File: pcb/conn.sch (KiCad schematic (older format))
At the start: 6 parts, among them P5 CONN_5X2, P6 CONN_16X2, P7 CONN_16, P8 CONN_32, P9 CONN_32

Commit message: almost finished with pcb design
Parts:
- removed P7: CONN_16, symbol CONN_16
- removed P8, P9: CONN_32, symbol CONN_32
- removed SD1: SD, symbol SD
- added JP10, JP2, JP3, JP4, JP5, JP7, JP8, JP9: JP_SW, JP_SW, symbol JP_SW
- added P2: CONN_16X2, symbol CONN_16X2
- renumbered P6 to P1, P5 to P3
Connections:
- net labels added: 0/MC0, 1/MC1, 10/MC10, 11/MC11, 12/MC12, 13/MC13, 14/MC14, 15/MC15, 16/SCL, 17/SDA, 18/EXTRA, 19/SATUS, 2/MC2, 3/MC3, 4/MC4, 5/MC5, 6/MC6, 7/MC7, 8/MC8, 9/MC9, USBDM0, USBDM1, USBDM2, USBDM3, USBDP0, USBDP1, USBDP2, USBDP3, USB_DM, USB_DP
- net labels removed: 0, 1, 10, 100/FSMC_D15, 11, 12, 13, 14, 15/SDIO_D0, 16/SDIO_D1, 17/SDIO_D2, 18/SDIO_D3, 19/SDIO_CK, 2, 20, 21, 22, 23, 24, 25, 26, 27/SDIO_CMD, 28, 29, 3, 30, 31, 32, 33, 34, 35, 36, 37, 38, 39, 4, 40, 41, 42, 43, 44, 45, 46, 47, 48, 49, 5, 50, 51, 52, 53, 54, 55, 56/FSMC_A0, 57/FSMC_A16, 58/FSMC_D0, 59/FSMC_A1, 6/BUT, 60/FSMC_A17, 61/FSMC_D1, 62/FSMC_A2, 63/FSMC_A18, 64/FSMC_D2, 65/FSMC_A3, 66/FSMC_A19, 67/FSMC_D3, 68/FSMC_A4, 69/FSMC_A20, 7, 70/FSMC_D4, 71/FSMC_A5, 72/FSMC_A21, 73/FSMC_D5, 74/FSMC_A6, 75/FSMC_A22, 76/FSMC_D6, 77/FSMC_A7, 78/FSMC_D7, 79/FSMC_A8, 8, 80/FSMC_NE2, 81/FSMC_D8, 82/FSMC_A9, 83/FSMC_NE3, 84/FSMC_D9, 85/FSMC_A10, 86/FSMC_NWE, 87/FSMC_D10, 88/FSMC_A11, 89/FSMC_NOE, 9, 90/FSMC_D11, 91/FSMC_A12, 92/FSMC_NBL1, 93/FSMC_D12, 94/FSMC_A13, 95/FSMC_NBL0, 96/FSMC_D13, 97/FSMC_A14, 98/FSMC_D14, 99/FSMC_A15, VREF
- wire segments 138 -> 105
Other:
- note added: "Bottom"
- note added: "Top"
- moved on the sheet: P1, P3

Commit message: working on power circuitry
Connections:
- net USBDM0: now also P1.23 (P23)
- net USBDM1: now also P1.25
- net USBDM2: now also P1.27 (P27)
- net USBDM3: now also P1.29 (P29)
- net USBDP0: now also P1.24 (P24)
- net USBDP1: now also P1.26 (P26)
- net USBDP2: now also P1.28 (P28)
- net USBDP3: now also P1.30 (P30)

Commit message: Work on single PCB version.
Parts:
- removed P2: CONN_16X2, symbol CONN_16X2
- added C10, C11, C12, C5, C6, C7, C8, C9, C? (x8): C, symbol C
- added P1: CONN_16X2, symbol CONN_16X2
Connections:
- net 0/MC0: now also C5.1, P1.3 (P3)
- net 1/MC1: now also C?.1, P1.4 (P4)
- net 10/MC10: now also C10.1, P1.13 (P13)
- net 11/MC11: now also C?.1, P1.14 (P14)
- net 12/MC12: now also C11.1, P1.15 (P15)
- net 13/MC13: now also C?.1, P1.16 (P16)
- net 14/MC14: now also C12.1, P1.17 (P17)
- net 15/MC15: now also C?.1, P1.18 (P18)
- net 16/SCL: now also P1.19 (P19)
- net 17/SDA: now also P1.20 (P20)
- net 18/EXTRA: now also P1.21 (P21)
- net 19/SATUS: now also P1.22 (P22)
- net 2/MC2: now also C6.1, P1.5 (P5)
- net 3/MC3: now also C?.1, P1.6 (P6)
- net 4/MC4: now also C7.1, P1.7 (P7)
- net 5/MC5: now also C?.1, P1.8 (P8)
- net 6/MC6: now also C8.1, P1.9 (P9)
- net 7/MC7: now also C?.1, P1.10 (P10)
- net 8/MC8: now also C9.1, P1.11 (P11)
- net 9/MC9: now also C?.1, P1.12 (P12)
- net GND: now also C8.2, C?.2, P1.2 (P2), P1.31 (P31)
- net USBDM0: now also P1.23 (P23)
- net USBDM1: now also P1.25
- net USBDM2: now also P1.27 (P27)
- net USBDM3: now also P1.29 (P29)
- net USBDP0: now also P1.24 (P24)
- net USBDP1: now also P1.26 (P26)
- net USBDP2: now also P1.28 (P28)
- net USBDP3: now also P1.30 (P30)
- net VCC: no longer P1.1 (P1), P1.32 (P32)
- new net: C10.2, C11.2, C12.2, C5.2, C6.2, C7.2, C9.2
- new net: C?.2, C?.2, C?.2, C?.2, C?.2, C?.2, C?.2
- new net VIN: P1.1 (P1), P1.1 (P1), P1.32 (P32), P1.32 (P32)
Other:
- moved on the sheet: JP10, JP2, JP3, JP4, JP5, JP7, JP8, JP9, P1, P3

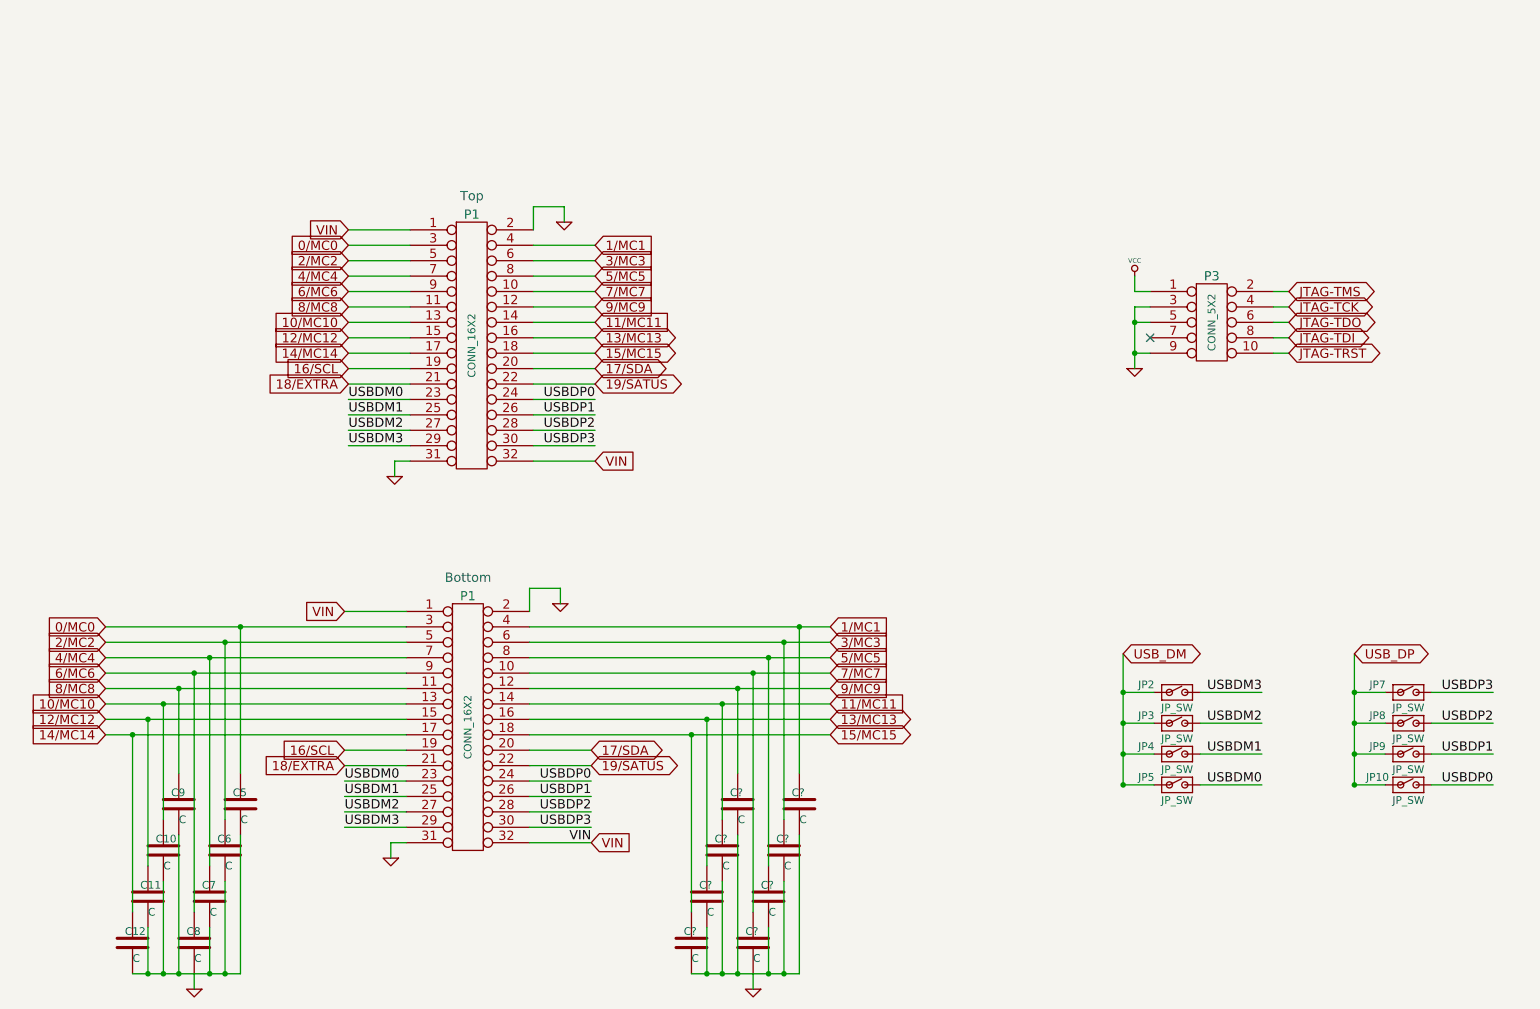
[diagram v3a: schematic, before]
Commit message: Re-routing new, single-board PCB
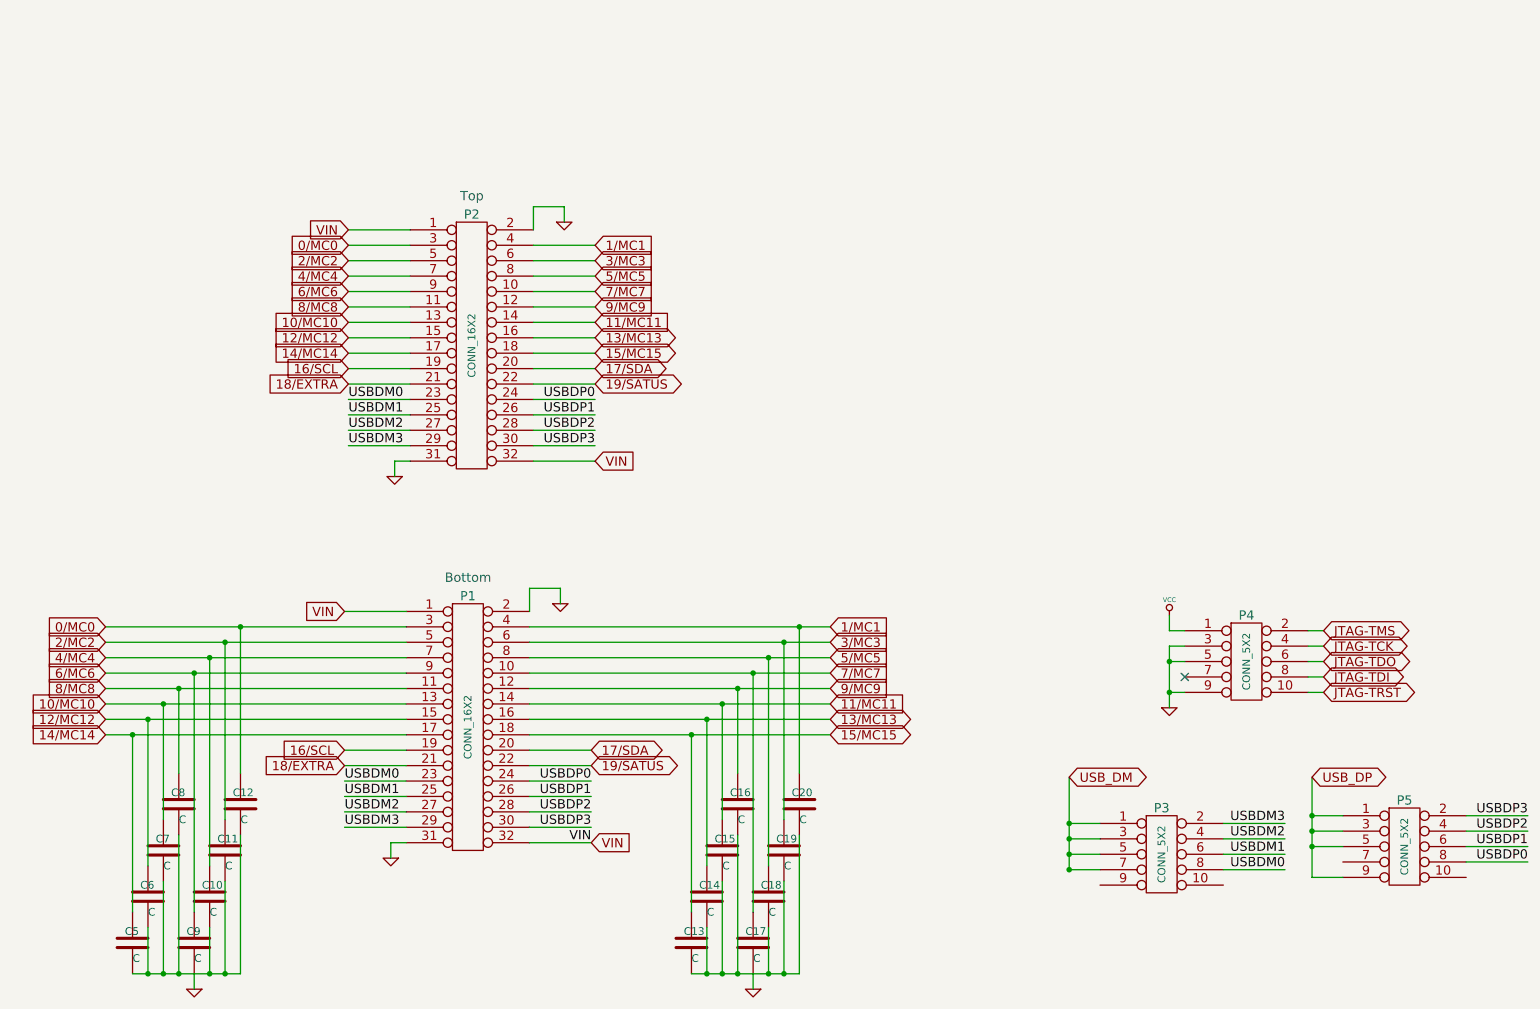
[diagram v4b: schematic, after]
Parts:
- removed JP10, JP2, JP3, JP4, JP5, JP7, JP8, JP9: JP_SW, JP_SW, symbol JP_SW
- added P3, P5: CONN_5X2, symbol CONN_5X2
- gave numbers to parts that had none: 8
- renumbered C7 to C10, C6 to C11, C5 to C12, C12 to C5, C11 to C6, C10 to C7, C9 to C8, C8 to C9, P1 to P2, P3 to P4
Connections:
- net USBDM0: now also P3.8
- net USBDM1: now also P3.6
- net USBDM2: now also P3.4
- net USBDM3: now also P3.2
- net USBDP0: now also P5.8
- net USBDP1: now also P5.6
- net USBDP2: now also P5.4
- net USBDP3: now also P5.2
- net USB_DM: now also P3.1, P3.3, P3.5, P3.7
- net USB_DP: now also P5.1, P5.3, P5.5, P5.9
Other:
- moved on the sheet: P4

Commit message: Board is routed!
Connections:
- net GND: now also C10.2, C11.2, C12.2, C13.2, C14.2, C15.2, C16.2, C18.2, C19.2, C20.2, C5.2, C6.2, C7.2, C8.2
- net USB_DP: now also P5.7; no longer P5.9
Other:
- moved on the sheet: C5, C8
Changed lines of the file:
@@
-EESchema Schematic File Version 2  date Wed 20 Mar 2013 06:41:12 PM PDT
+EESchema Schematic File Version 2  date Fri 22 Mar 2013 07:46:03 PM PDT
 LIBS:power
 LIBS:device
@@
 LIBS:led_16x16
 LIBS:uA7800
+LIBS:miniusb
 LIBS:panels_g4-cache
 EELAYER 25  0
@@
 Sheet 4 5
 Title ""
-Date "21 mar 2013"
+Date "22 mar 2013"
 Rev ""
 Comp ""
@@
 Comment4 ""
 $EndDescr
+Wire Wire Line
+	2250 5700 2250 5125
+Connection ~ 5975 7035
+Wire Wire Line
+	1950 7030 2650 7030
+Wire Wire Line
+	1950 7030 1950 7000
+Connection ~ 2350 7030
+Wire Wire Line
+	9800 6250 9600 6250
 Connection ~ 9600 6050
 Connection ~ 8025 6200
@@
 Connection ~ 6075 4925
 Connection ~ 6275 4725
-Connection ~ 2150 6975
-Wire Wire Line
-	2150 6975 2150 6375
-Wire Wire Line
-	1950 6975 2650 6975
-Connection ~ 2550 6975
-Wire Wire Line
-	2550 6375 2550 6975
-Wire Wire Line
-	2350 6975 2350 7075
-Wire Wire Line
-	1950 6575 1950 5425
+Connection ~ 2150 7030
+Wire Wire Line
+	2150 7030 2150 6375
+Connection ~ 2550 7030
+Wire Wire Line
+	2550 6375 2550 7030
+Wire Wire Line
+	1950 6600 1950 5425
 Wire Wire Line
 	2150 5975 2150 5225
@@
 Wire Wire Line
 	10600 6150 11000 6150
-Wire Wire Line
-	9800 6350 9600 6350
 Connection ~ 9600 6150
 Wire Wire Line
@@
 Connection ~ 9600 5950
 Wire Wire Line
-	9600 6350 9600 5700
-Wire Wire Line
 	9025 6200 9425 6200
 Wire Wire Line
@@
 	4950 2250 4550 2250
 Wire Wire Line
-	4525 4725 6475 4725
-Wire Wire Line
-	4525 4925 6475 4925
-Wire Wire Line
-	4525 5125 6475 5125
-Wire Wire Line
-	4525 5325 6475 5325
+	6475 4725 4525 4725
+Wire Wire Line
+	6475 4925 4525 4925
+Wire Wire Line
+	6475 5125 4525 5125
+Wire Wire Line
+	6475 5325 4525 5325
 Wire Wire Line
 	4925 5925 4525 5925
@@
 	4525 4475 4725 4475
 Wire Wire Line
-	4525 5425 6475 5425
+	6475 5425 4525 5425
 Wire Wire Line
 	4925 5525 4525 5525
@@
 	3325 5525 3725 5525
 Wire Wire Line
-	1775 5325 3725 5325
-Wire Wire Line
-	1775 5125 3725 5125
-Wire Wire Line
-	1775 4925 3725 4925
-Wire Wire Line
-	1775 4725 3725 4725
-Wire Wire Line
-	1775 4825 3725 4825
-Wire Wire Line
-	1775 5025 3725 5025
-Wire Wire Line
-	1775 5225 3725 5225
-Wire Wire Line
-	1775 5425 3725 5425
+	3725 5325 1775 5325
+Wire Wire Line
+	3725 5125 1775 5125
+Wire Wire Line
+	3725 4925 1775 4925
+Wire Wire Line
+	3725 4725 1775 4725
+Wire Wire Line
+	3725 4825 1775 4825
+Wire Wire Line
+	3725 5025 1775 5025
+Wire Wire Line
+	3725 5225 1775 5225
+Wire Wire Line
+	3725 5425 1775 5425
 Wire Wire Line
 	3325 5625 3725 5625
@@
 	4925 5825 4525 5825
 Wire Wire Line
-	4525 5225 6475 5225
-Wire Wire Line
-	4525 5025 6475 5025
-Wire Wire Line
-	4525 4825 6475 4825
+	6475 5225 4525 5225
+Wire Wire Line
+	6475 5025 4525 5025
+Wire Wire Line
+	6475 4825 4525 4825
 Wire Wire Line
 	4925 6125 4525 6125
@@
 	8675 4750 8775 4750
 Wire Wire Line
-	2650 4725 2650 5675
+	2650 5675 2650 4725
 Connection ~ 2650 4725
 Connection ~ 2150 5225
-Wire Wire Line
-	2250 5675 2250 5125
 Connection ~ 2350 5025
 Wire Wire Line
@@
 	2050 6275 2050 5325
 Wire Wire Line
-	2650 6975 2650 6075
-Wire Wire Line
-	2450 6675 2450 6975
-Connection ~ 2450 6975
-Wire Wire Line
-	2050 6675 2050 6975
-Connection ~ 2050 6975
-Wire Wire Line
-	2250 6075 2250 6975
-Connection ~ 2250 6975
-Connection ~ 5875 6975
-Wire Wire Line
-	5875 6975 5875 6075
-Connection ~ 5675 6975
-Wire Wire Line
-	5675 6975 5675 6675
-Connection ~ 6075 6975
-Wire Wire Line
-	6075 6975 6075 6675
-Wire Wire Line
-	6275 6075 6275 6975
+	2650 7030 2650 6075
+Wire Wire Line
+	2450 7030 2450 6675
+Connection ~ 2450 7030
+Wire Wire Line
+	2050 7030 2050 6675
+Connection ~ 2050 7030
+Wire Wire Line
+	2250 7030 2250 6100
+Connection ~ 5875 7035
+Wire Wire Line
+	5875 7035 5875 6075
+Connection ~ 5675 7035
+Wire Wire Line
+	5675 6675 5675 7035
+Connection ~ 6075 7035
+Wire Wire Line
+	6075 7035 6075 6675
+Wire Wire Line
+	6275 6075 6275 7035
 Wire Wire Line
 	5675 6275 5675 5325
@@
 	5875 5675 5875 5125
 Wire Wire Line
-	6275 4725 6275 5675
+	6275 5675 6275 4725
 Wire Wire Line
 	6075 6275 6075 4925
@@
 	5575 6575 5575 5425
 Wire Wire Line
-	5975 6975 5975 7075
-Wire Wire Line
-	6175 6375 6175 6975
-Connection ~ 6175 6975
-Wire Wire Line
-	6275 6975 5575 6975
-Wire Wire Line
-	5775 6975 5775 6375
-Connection ~ 5775 6975
+	6175 7035 6175 6375
+Connection ~ 6175 7035
+Wire Wire Line
+	5775 7035 5775 6375
+Connection ~ 5775 7035
 Connection ~ 6175 4825
 Connection ~ 5975 5025
@@
 	8025 6300 8025 5700
 Connection ~ 8025 6000
-Connection ~ 8025 6300
+Wire Wire Line
+	9600 6250 9600 5700
+Connection ~ 2250 7030
+Wire Wire Line
+	2350 6975 2350 7075
+Wire Wire Line
+	5575 6975 5575 7035
+Wire Wire Line
+	5575 7035 6275 7035
+Wire Wire Line
+	5975 7075 5975 6975
 $Comp
 L CONN_5X2 P5
@@
 L C C5
 U 1 1 513F7F31
-P 1950 6775
-F 0 "C5" H 1900 6850 50  0000 L CNN
-F 1 "C" H 1950 6675 50  0000 L CNN
-	1    1950 6775
+P 1950 6800
+F 0 "C5" H 1900 6875 50  0000 L CNN
+F 1 "C" H 1950 6700 50  0000 L CNN
+	1    1950 6800
 	1    0    0    -1
 $EndComp
@@
 L C C8
 U 1 1 513F7F30
-P 2250 5875
-F 0 "C8" H 2200 5950 50  0000 L CNN
-F 1 "C" H 2250 5775 50  0000 L CNN
-	1    2250 5875
-	1    0    0    -1
-$EndComp
+P 2250 5900
+F 0 "C8" H 2200 5975 50  0000 L CNN
+F 1 "C" H 2250 5800 50  0000 L CNN
+	1    2250 5900
+	1    0    0    -1
+$EndComp

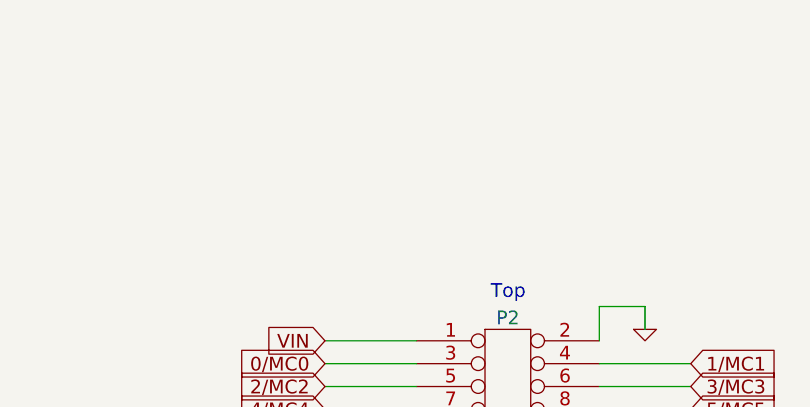
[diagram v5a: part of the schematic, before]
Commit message: Added mounting holes
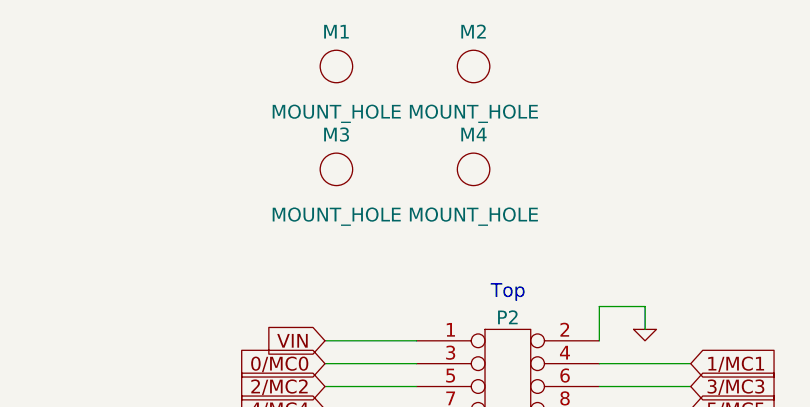
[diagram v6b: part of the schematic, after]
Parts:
- added M1, M2, M3, M4: MOUNT_HOLE, symbol MOUNT_HOLE
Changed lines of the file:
@@
-EESchema Schematic File Version 2  date Fri 22 Mar 2013 07:46:03 PM PDT
+EESchema Schematic File Version 2  date Mon 25 Mar 2013 08:21:12 AM PDT
 LIBS:power
 LIBS:device
@@
 LIBS:uA7800
 LIBS:miniusb
+LIBS:mount_hole
 LIBS:panels_g4-cache
 EELAYER 25  0
@@
 Sheet 4 5
 Title ""
-Date "22 mar 2013"
+Date "25 mar 2013"
 Rev ""
 Comp ""
@@
 Comment4 ""
 $EndDescr
+$Comp
+L MOUNT_HOLE M1
+U 1 1 51506B41
+P 3400 950
+F 0 "M1" H 3400 1100 60  0000 C CNN
+F 1 "MOUNT_HOLE" H 3400 750 60  0000 C CNN
+	1    3400 950
+	1    0    0    -1
+$EndComp
+$Comp
+L MOUNT_HOLE M2
+U 1 1 51506B40
+P 4000 950
+F 0 "M2" H 4000 1100 60  0000 C CNN
+F 1 "MOUNT_HOLE" H 4000 750 60  0000 C CNN
+	1    4000 950
+	1    0    0    -1
+$EndComp
+$Comp
+L MOUNT_HOLE M4
+U 1 1 51506B37
+P 4000 1400
+F 0 "M4" H 4000 1550 60  0000 C CNN
+F 1 "MOUNT_HOLE" H 4000 1200 60  0000 C CNN
+	1    4000 1400
+	1    0    0    -1
+$EndComp
+$Comp
+L MOUNT_HOLE M3
+U 1 1 51506B2C
+P 3400 1400
+F 0 "M3" H 3400 1550 60  0000 C CNN
+F 1 "MOUNT_HOLE" H 3400 1200 60  0000 C CNN
+	1    3400 1400
+	1    0    0    -1
+$EndComp
 Wire Wire Line
 	2250 5700 2250 5125
